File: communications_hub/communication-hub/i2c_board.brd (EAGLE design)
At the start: 82.5 x 54 mm, 40 parts, among them CON3 SM03B-GHS-TB, CON4 SM03B-GHS-TB, U3 TCAN1042HVDR, U4 TCAN1042HVDR

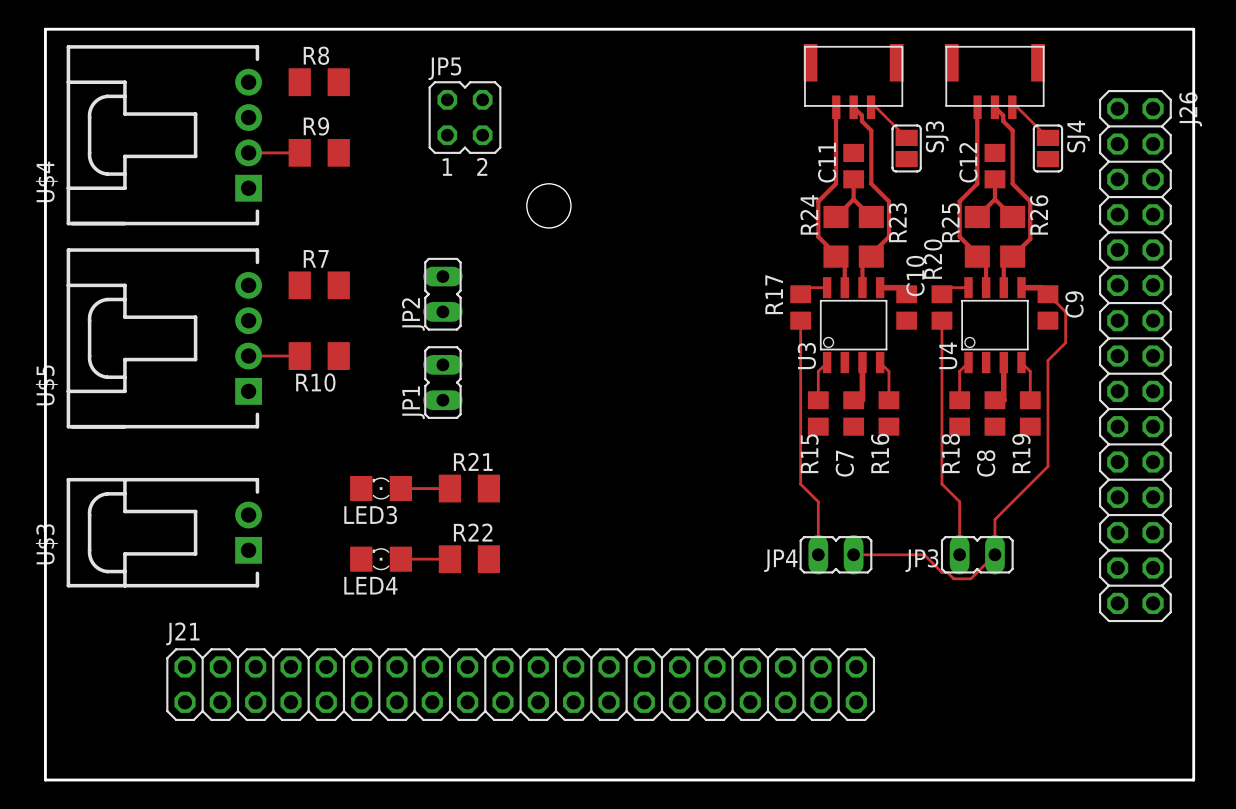
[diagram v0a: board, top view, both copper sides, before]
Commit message: Fine tuned positions of 30 and 40 pin headers
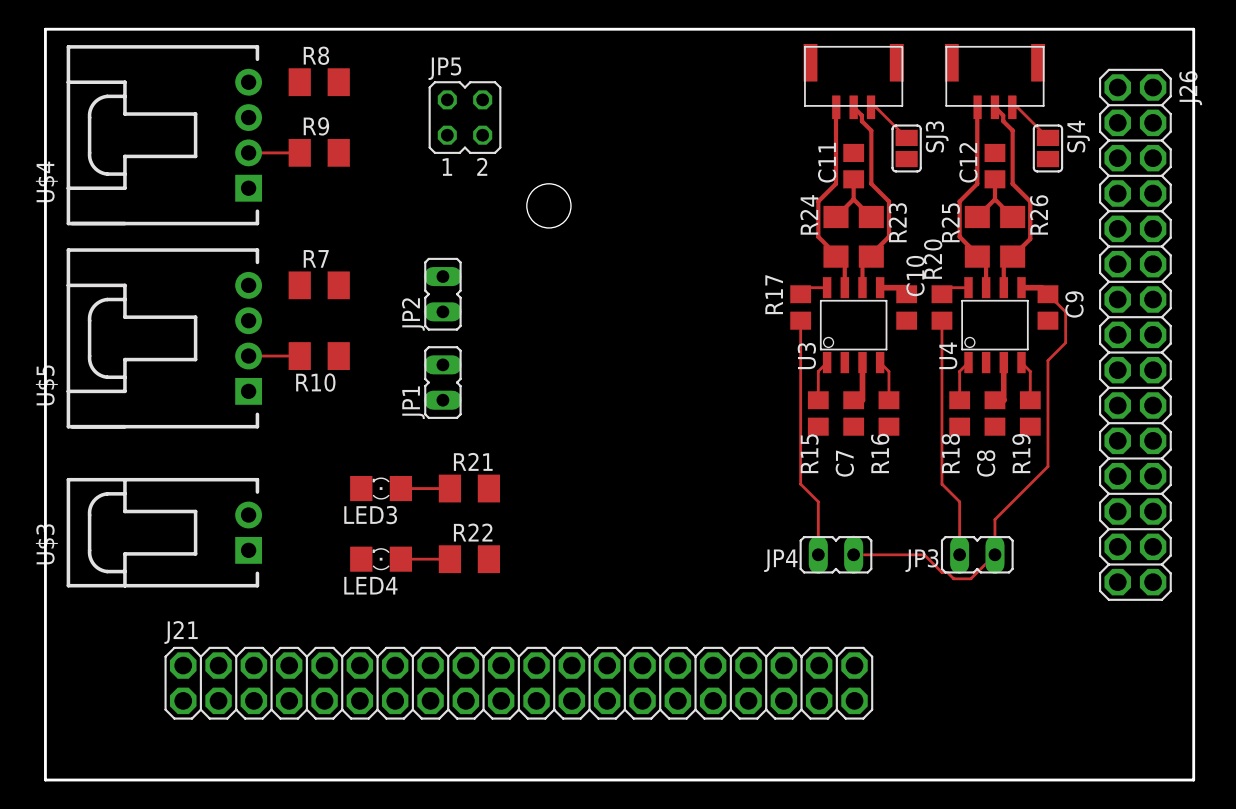
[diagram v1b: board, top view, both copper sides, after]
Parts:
- J21: device pinhead:2X20 -> commhub:2X20
- J26: device pinhead:2X15 -> commhub:2X15
- moved J26 1.52 mm to (78.4, 32.0)
- moved J21 0.16 mm to (34.0, 6.96)

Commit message: Finished first revision of communication hub board. Needs to be reviewed before commit.
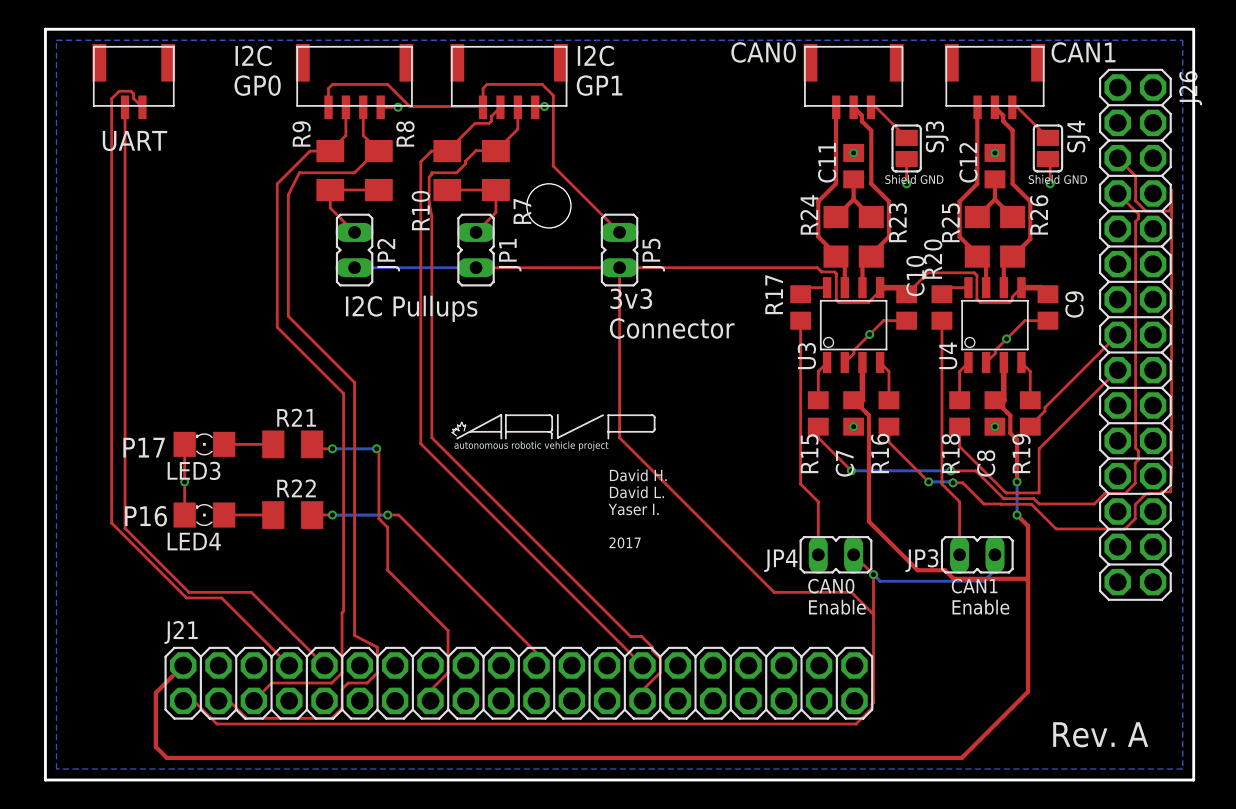
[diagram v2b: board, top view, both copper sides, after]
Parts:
- removed U$3: MOLEX_SL_02-70553, molex-sl-connectors_jw:SL_70553_2
- removed U$4, U$5: MOLEX_SL_04-70553, molex-sl-connectors_jw:SL_70553_4
- added CON1, CON2: SM04B-GHS-TB, ARVP:SM04B-GHS-TB
- added CON5: SM02B-GHS-TB, ARVP:SM02B-GHS-TB
- added U$1: (no value), ARVP:ARVP
- JP5: device jumper:JP2Q -> jumper:JP1
- moved R10 16.2 mm to (28.9, 43.8), turned to 90 degrees
- moved R7 15.1 mm to (32.4, 43.8), turned to 270 degrees
- moved JP5 14.6 mm to (41.3, 38.1), turned to 180 degrees
- moved LED3 13.1 mm to (11.4, 24.1)
- moved LED4 13.1 mm to (11.4, 19.1)
- moved R21 13.1 mm to (17.8, 24.1)
- moved R22 13.1 mm to (17.8, 19.1)
- moved JP1 9.82 mm to (31.0, 38.1), turned to 180 degrees
- moved R8 7.66 mm to (24.0, 43.8), turned to 270 degrees
- moved JP2 7.10 mm to (22.2, 38.1), turned to 180 degrees
- moved R9 1.50 mm to (20.5, 43.8), turned to 270 degrees
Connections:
- net +3V3: now also J21.1, JP1.2, JP2.2, JP5.2; no longer JP5.3
- net +5V: now also J21.2
- net CAN0_TX_T: now also J26.7
- net CAN1_TX_T: no longer J26.7
- net GND: now also CON1.P$1, CON2.P$1, J21.14, J21.20, J21.25, J21.30, J21.34, J21.35, J21.6, J21.9; no longer U$4.4, U$5.4
- net I2C_GP0_SCL: now also CON2.P$3; no longer U$4.2
- net I2C_GP0_SDA: now also CON2.P$2; no longer U$4.3
- net I2C_GP1_SCL: now also CON1.P$3; no longer U$5.2
- net I2C_GP1_SDA: now also CON1.P$2; no longer U$5.3
- net N$6: now also CON1.P$4, CON2.P$4; no longer U$4.1, U$5.1
- net UART1_RX: now also CON5.P$2; no longer U$3.1
- net UART1_TX: now also CON5.P$1; no longer U$3.2
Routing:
- net +3V3: track 37.4 -> 165.0 mm, vias 0 -> 1
- net +5V: track 6.69 -> 122.7 mm, vias 0 -> 2
- net I2C_GP0_SDA: track 0.00 -> 63.1 mm
- net CAN0_RX_T: track 0.00 -> 55.3 mm, vias 0 -> 2
- net I2C_GP1_SDA: track 0.00 -> 55.1 mm
- net UART1_TX: track 0.00 -> 50.6 mm
- net I2C_GP0_SCL: track 3.68 -> 52.7 mm
- net UART1_RX: track 0.00 -> 48.7 mm
- net CAN0_TX_T: track 0.00 -> 47.9 mm, vias 0 -> 2
- net I2C_GP1_SCL: track 3.68 -> 50.4 mm
- net N$6: track 0.00 -> 31.9 mm
- net GPIO_EXP_P17: track 0.00 -> 25.5 mm, vias 0 -> 2
- net GND: track 0.00 -> 22.9 mm, vias 0 -> 11
- net GPIO_EXP_P16: track 0.00 -> 21.1 mm, vias 0 -> 2
- net CAN1_TX_T: track 0.00 -> 19.7 mm
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- added copper zone on layer 16, net GND
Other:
- board text added: "2017"
- board text added: "3v3 Connector"
- board text added: "CAN0"
- board text added: "CAN0 Enable"
- board text added: "CAN1"
- board text added: "CAN1 Enable"
- board text added: "David H. David L. Yaser I."
- board text added: "I2C GP0"
- board text added: "I2C GP1"
- board text added: "I2C Pullups"
- board text added: "P16"
- board text added: "P17"
- board text added: "Rev. A"
- board text added: "Shield GND"
- board text added: "UART"

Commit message: Made requisite changes to communications hub.
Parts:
- added JP6: (no value), jumper:JP1
- moved JP5 27.1 mm to (14.2, 37.8)
- renumbered LED3 to LED1, LED4 to LED2
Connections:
- new net N$5: CON1.P$4, JP6.1
- net +3V3: now also JP6.2
- net N$6: no longer CON1.P$4
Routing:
- net N$6: track 31.9 -> 11.9 mm
- net N$5: track 0.00 -> 19.6 mm
- net GND: track 22.9 -> 6.87 mm, vias 11 -> 3
- net +3V3: track 165.0 -> 180.8 mm, vias 1 -> 4
- net +5V: track 122.7 -> 124.1 mm
- net UART1_TX: track 50.6 -> 51.7 mm
- net GPIO_EXP_P17: track 25.5 -> 26.3 mm
- added copper zone on layer 1, net GND
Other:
- board text added: "3v3 to Connector"
- board text added: "Communications Hub"
- board text removed: "3v3 Connector"
